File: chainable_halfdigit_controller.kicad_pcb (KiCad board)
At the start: 2 copper layers, 100 x 40 mm, 12 parts, among them J1 USB_OTG, J2 Conn_01x06, J3 Conn_01x01, J4 Conn_01x01, SW1 SW_SPST, U1 NRF24L01, U2 arduino_nano

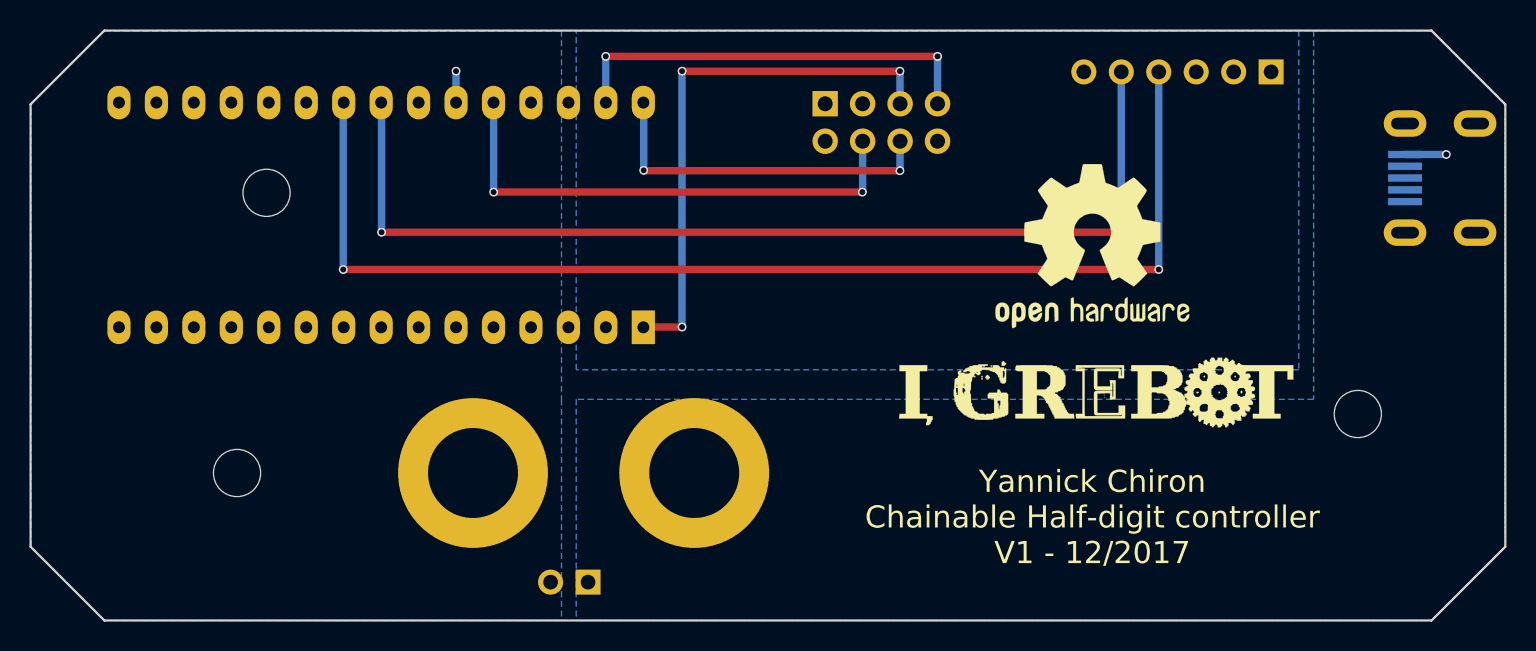
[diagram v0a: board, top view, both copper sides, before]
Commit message: Fixed DRC errors
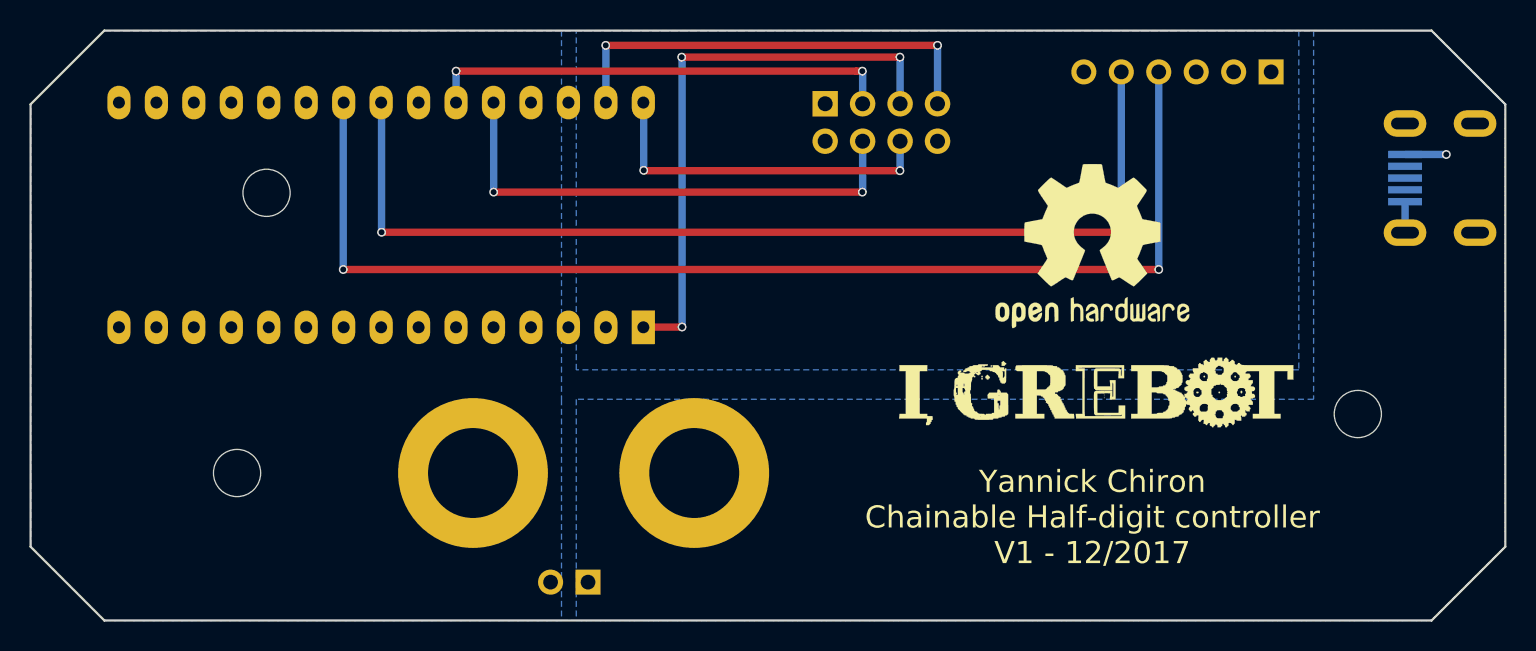
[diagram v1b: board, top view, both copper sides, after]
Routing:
- net CE: track 2.13 -> 31.9 mm, vias 1 -> 2
- net GND: track 0.00 -> 2.10 mm, vias 0 -> 1
- net SCK: track 37.0 -> 38.9 mm
- net MISO: track 29.2 -> 30.7 mm
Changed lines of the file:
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@@
   (general
     (links 21)
-    (no_connects 2)
+    (no_connects 0)
     (area 49.924999 49.924999 152.075 90.861905)
     (thickness 1.6)
     (drawings 9)
-    (tracks 48)
+    (tracks 57)
     (zones 0)
     (modules 12)
@@
   (gr_line (start 55 50) (end 145 50) (layer Edge.Cuts) (width 0.15))
   (gr_line (start 50 55) (end 55 50) (layer Edge.Cuts) (width 0.15))
-  (segment (start 89 51.75) (end 89 54.87) (width 0.5) (layer B.Cu) (net 6))
+  (segment (start 143.2 61.6) (end 143.2 63.7) (width 0.5) (layer B.Cu) (net 1))
+  (via (at 143.2 63.7) (size 0.6) (drill 0.4) (layers F.Cu B.Cu) (net 1))
+  (segment (start 89.01 54.88) (end 89.01 51.01) (width 0.5) (layer B.Cu) (net 6))
+  (segment (start 89.01 51.01) (end 89 51) (width 0.5) (layer B.Cu) (net 6))
+  (segment (start 111.5 51) (end 89 51) (width 0.5) (layer F.Cu) (net 6))
+  (via (at 89 51) (size 0.6) (drill 0.4) (layers F.Cu B.Cu) (net 6))
+  (segment (start 111.5 54.96) (end 111.5 51) (width 0.5) (layer B.Cu) (net 6))
+  (via (at 111.5 51) (size 0.6) (drill 0.4) (layers F.Cu B.Cu) (net 6))
   (segment (start 89 54.87) (end 89.01 54.88) (width 0.5) (layer B.Cu) (net 6))
-  (segment (start 111.5 51.75) (end 89 51.75) (width 0.5) (layer F.Cu) (net 6))
-  (via (at 89 51.75) (size 0.6) (drill 0.4) (layers F.Cu B.Cu) (net 6))
-  (segment (start 111.5 54.96) (end 111.5 51.75) (width 0.5) (layer B.Cu) (net 6))
-  (via (at 111.5 51.75) (size 0.6) (drill 0.4) (layers F.Cu B.Cu) (net 6))
   (segment (start 89.01 54.5244) (end 89.01 54.88) (width 0.5) (layer F.Cu) (net 6))
+  (segment (start 94.175 70.1) (end 94.175 51.825) (width 0.5) (layer B.Cu) (net 7))
+  (segment (start 94.175 51.825) (end 94.15 51.8) (width 0.5) (layer B.Cu) (net 7))
+  (segment (start 108.95 51.8) (end 94.15 51.8) (width 0.5) (layer F.Cu) (net 7))
+  (via (at 94.15 51.8) (size 0.6) (drill 0.4) (layers F.Cu B.Cu) (net 7))
+  (segment (start 108.96 54.96) (end 108.96 51.81) (width 0.5) (layer B.Cu) (net 7))
+  (segment (start 108.96 51.81) (end 108.95 51.8) (width 0.5) (layer B.Cu) (net 7))
+  (via (at 108.95 51.8) (size 0.6) (drill 0.4) (layers F.Cu B.Cu) (net 7))
   (segment (start 94.175 70.1) (end 91.57 70.1) (width 0.5) (layer F.Cu) (net 7))
   (segment (start 91.57 70.1) (end 91.55 70.12) (width 0.5) (layer F.Cu) (net 7))
   (via (at 94.175 70.1) (size 0.6) (drill 0.4) (layers F.Cu B.Cu) (net 7))
-  (segment (start 94.175 52.75) (end 94.175 70.1) (width 0.5) (layer B.Cu) (net 7))
-  (segment (start 108.95 52.75) (end 94.175 52.75) (width 0.5) (layer F.Cu) (net 7))
-  (via (at 94.175 52.75) (size 0.6) (drill 0.4) (layers F.Cu B.Cu) (net 7))
-  (segment (start 108.96 54.96) (end 108.96 52.76) (width 0.5) (layer B.Cu) (net 7))
-  (segment (start 108.96 52.76) (end 108.95 52.75) (width 0.5) (layer B.Cu) (net 7))
-  (via (at 108.95 52.75) (size 0.6) (drill 0.4) (layers F.Cu B.Cu) (net 7))
   (segment (start 91.575 59.475) (end 91.575 54.905) (width 0.5) (layer B.Cu) (net 8))
   (segment (start 91.575 54.905) (end 91.55 54.88) (width 0.5) (layer B.Cu) (net 8))
@@
   (segment (start 108.96 59.49) (end 108.95 59.5) (width 0.5) (layer B.Cu) (net 8))
   (via (at 108.95 59.5) (size 0.6) (drill 0.4) (layers F.Cu B.Cu) (net 8))
+  (segment (start 106.4 52.75) (end 105.975736 52.75) (width 0.5) (layer F.Cu) (net 9))
+  (segment (start 105.975736 52.75) (end 78.85 52.75) (width 0.5) (layer F.Cu) (net 9))
+  (segment (start 106.42 54.96) (end 106.42 52.77) (width 0.5) (layer B.Cu) (net 9))
+  (segment (start 106.42 52.77) (end 106.4 52.75) (width 0.5) (layer B.Cu) (net 9))
+  (via (at 106.4 52.75) (size 0.6) (drill 0.4) (layers F.Cu B.Cu) (net 9))
   (segment (start 78.85 52.75) (end 78.85 54.88) (width 0.5) (layer B.Cu) (net 9))
   (via (at 78.85 52.75) (size 0.6) (drill 0.4) (layers F.Cu B.Cu) (net 9))
@@
   (segment (start 123.95 63.675) (end 73.8 63.675) (width 0.5) (layer F.Cu) (net 33))
   (segment (start 73.8 54.91) (end 73.77 54.88) (width 0.5) (layer B.Cu) (net 33))
+  (via (at 146 58.4) (size 0.6) (drill 0.4) (layers F.Cu B.Cu) (net 36))
   (segment (start 143.2 58.4) (end 146 58.4) (width 0.5) (layer B.Cu) (net 36))
-  (via (at 146 58.4) (size 0.6) (drill 0.4) (layers F.Cu B.Cu) (net 36))
   (zone (net 3) (net_name 5V) (layer B.Cu) (hatch edge 0.508)
     (connect_pads (clearance 0.508))

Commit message: Added via near USB GND pin
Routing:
- net GND: track 2.10 -> 4.90 mm, vias 1 -> 2
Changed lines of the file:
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@@
     (thickness 1.6)
     (drawings 9)
-    (tracks 57)
+    (tracks 59)
     (zones 0)
     (modules 12)
@@
   (gr_line (start 55 50) (end 145 50) (layer Edge.Cuts) (width 0.15))
   (gr_line (start 50 55) (end 55 50) (layer Edge.Cuts) (width 0.15))
+  (segment (start 143.2 61.6) (end 146 61.6) (width 0.5) (layer B.Cu) (net 1))
+  (via (at 146 61.6) (size 0.6) (drill 0.4) (layers F.Cu B.Cu) (net 1))
   (segment (start 143.2 61.6) (end 143.2 63.7) (width 0.5) (layer B.Cu) (net 1))
   (via (at 143.2 63.7) (size 0.6) (drill 0.4) (layers F.Cu B.Cu) (net 1))
